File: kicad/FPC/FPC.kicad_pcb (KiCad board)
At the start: 2 copper layers, 29.3 x 5 mm, 2 parts, among them J1 Conn_01x04_Pin, J2 Conn_01x04_Pin

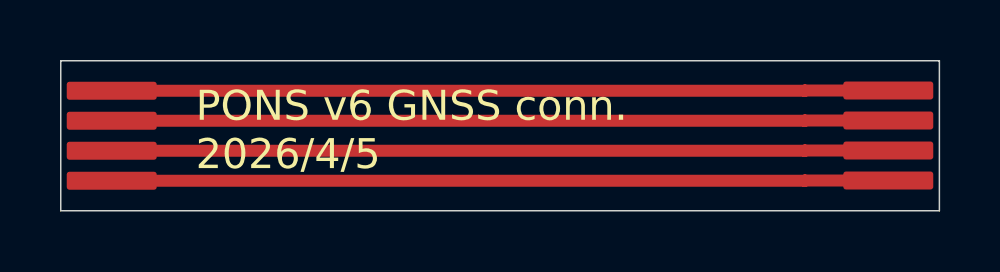
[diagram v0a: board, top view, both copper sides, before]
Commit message: 0.960 ソフトウェア＋ドキュメント KiCad v7 基板
普段編集しないモジュールを src/ へ移動し、README を v7 に更新

■ src/ への移動（Arduino IDE のタブ削減）
Arduino IDE はスケッチ直下のファイルを全部タブに出すため 28 個まで増え、
目的のファイルを探しづらくなっていた。仕様が固まっていて普段いじらない
4 モジュールを src/ へ移し、タブを 20 個に減らした。

  src/button.*     ボタン入力・メニュー
  src/sound.*      音声出力（WAV・トーン）
  src/vectormap.*  ベクタ地図の描画
  src/imulog.*     生 IMU ロガー

src/ 配下もコンパイルされるが IDE のタブには出ない。裏を返すと IDE からは
編集できなくなるので、これらは VSCode 等で編集すること。
またスケッチ直下は include パスに入っていないため、src/ の中からルート側の
ヘッダを参照するときは "../mysd.h" のように 1 段戻る必要がある。
この経緯と注意点は GPS_TFT_map.ino のヘッダに残した。

#include は 27 箇所を書き換え、全 104 件が実在するパスへ解決することを確認。

■ 併せて修正
button.cpp の #include "Button.h" が大文字始まりだった。macOS は
ファイルシステムが大文字小文字を区別しないため通っていたが、Linux では
壊れる。"button.h" に修正。

■ README を v7 に更新
 * タイトルとスペックを v7 へ。ソフトウェアバージョン 0.942 → 0.960
 * PONS Link（機体⇄ボート テレメトリ無線）の節を新設。3 台構成、下り一方向に
   した理由、無線パラメータ、実測 350m。設計の詳細は docs/pons_link.md へ
 * BNO085 を β 試験版から標準搭載へ。SPI 接続にした理由も記載
 * マイコンを RP2350B（外付け FLASH 16MB）と明記
 * PCBA とは別に発注する部品の一覧表（Digikey / マルツ / 秋月）を追加
 * 警告音・SD ログ・使用部品に無線関連を追記

重量とバッテリー持続時間は v7 実機での計測待ちのため、v6 β版の参考値と
PONS Link の消費電流だけを記載した。水面での到達距離も未確認と明記。

普段編集しないモジュールを src/ へ移動し、README を v7 に更新

■ src/ への移動（Arduino IDE のタブ削減）
Arduino IDE はスケッチ直下のファイルを全部タブに出すため 28 個まで増え、
目的のファイルを探しづらくなっていた。仕様が固まっていて普段いじらない
4 モジュールを src/ へ移し、タブを 20 個に減らした。

  src/button.*     ボタン入力・メニュー
  src/sound.*      音声出力（WAV・トーン）
  src/vectormap.*  ベクタ地図の描画
  src/imulog.*     生 IMU ロガー

src/ 配下もコンパイルされるが IDE のタブには出ない。裏を返すと IDE からは
編集できなくなるので、これらは VSCode 等で編集すること。
またスケッチ直下は include パスに入っていないため、src/ の中からルート側の
ヘッダを参照するときは "../mysd.h" のように 1 段戻る必要がある。
この経緯と注意点は GPS_TFT_map.ino のヘッダに残した。

#include は 27 箇所を書き換え、全 104 件が実在するパスへ解決することを確認。

■ 併せて修正
button.cpp の #include "Button.h" が大文字始まりだった。macOS は
ファイルシステムが大文字小文字を区別しないため通っていたが、Linux では
壊れる。"button.h" に修正。

■ README を v7 に更新
 * タイトルとスペックを v7 へ。ソフトウェアバージョン 0.942 → 0.960
 * PONS Link（機体⇄ボート テレメトリ無線）の節を新設。3 台構成、下り一方向に
   した理由、無線パラメータ、実測 350m。設計の詳細は docs/pons_link.md へ
 * BNO085 を β 試験版から標準搭載へ。SPI 接続にした理由も記載
 * マイコンを RP2350B（外付け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
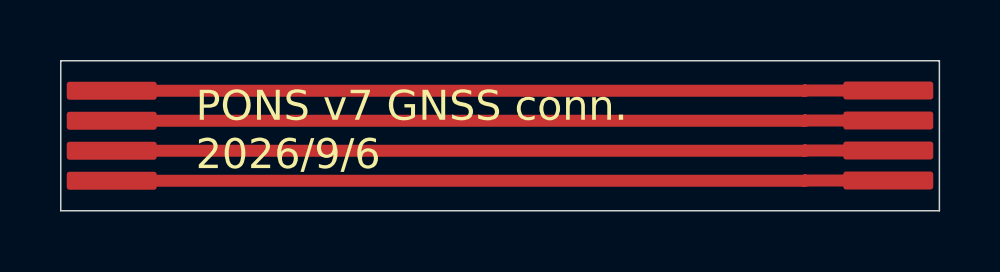
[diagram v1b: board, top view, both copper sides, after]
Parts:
- J1, J2: footprint PONS:FPC_CON 4 POS 1mm -> FPC_CON 4p 1mm:FPC_CON 4p 1mm
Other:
- board text added: "PONS v7 GNSS conn. 2026/9/6"
- board text added: "Stiffener: Polyimide Thickness: 0.3mm"
- board text removed: "PONS v6 GNSS conn. 2026/4/5"
- board text removed: "Stiffener: Polyimide Thickness: 0.25mm or 0.3mm"
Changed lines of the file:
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@@
 (kicad_pcb
-	(version 20241229)
+	(version 20260206)
 	(generator "pcbnew")
-	(generator_version "9.0")
+	(generator_version "10.0")
 	(general
 		(thickness 1.6)
@@
 	)
 	(paper "A4")
+	(title_block
+		(title "FPC for PONS v7")
+		(date "2026-09-06")
+		(rev "v7")
+		(comment 1 "EXPORT Stiffener AND User.Comments for JLCPCB")
+	)
 	(layers
 		(0 "F.Cu" signal)
@@
 		(pad_to_mask_clearance 0)
 		(allow_soldermask_bridges_in_footprints no)
-		(tenting front back)
+		(tenting
+			(front yes)
+			(back yes)
+		)
+		(covering
+			(front no)
+			(back no)
+		)
+		(plugging
+			(front no)
+			(back no)
+		)
+		(capping no)
+		(filling no)
 		(pcbplotparams
 			(layerselection 0x00000000_00000000_5555d555_5755f5ff)
@@
 			(usegerberadvancedattributes no)
 			(creategerberjobfile no)
-			(dashed_line_dash_ratio 12.000000)
-			(dashed_line_gap_ratio 3.000000)
+			(dashed_line_dash_ratio 12)
+			(dashed_line_gap_ratio 3)
 			(svgprecision 4)
 			(plotframeref no)
 			(mode 1)
 			(useauxorigin no)
-			(hpglpennumber 1)
-			(hpglpenspeed 20)
-			(hpglpendiameter 15.000000)
 			(pdf_front_fp_property_popups yes)
 			(pdf_back_fp_property_popups yes)
@@
 		)
 	)
-	(net 0 "")
-	(net 1 "Net-(J1-Pin_4)")
-	(net 2 "Net-(J1-Pin_1)")
-	(net 3 "Net-(J1-Pin_3)")
-	(net 4 "Net-(J1-Pin_2)")
-	(footprint "PONS:FPC_CON 4 POS 1mm"
+	(footprint "FPC_CON 4p 1mm:FPC_CON 4p 1mm"
 		(layer "F.Cu")
 		(at 120.6 66.2)
@@
 			)
 		)
-		(property "Datasheet" "~"
+		(property "Datasheet" ""
 			(at 0 0 0)
 			(unlocked yes)
@@
 		(sheetname "/")
 		(sheetfile "FPC.kicad_sch")
+		(units
+			(unit
+				(name "A")
+				(pins "1" "2" "3" "4")
+			)
+		)
 		(attr smd)
+		(duplicate_pad_numbers_are_jumpers no)
 		(fp_text user "${REFERENCE}"
 			(at 0 2.5 0)
@@
 			(layers "F.Cu" "F.Mask" "F.Paste")
 			(roundrect_rratio 0.15)
-			(net 2 "Net-(J1-Pin_1)")
-			(pinfunction "Pin_1")
+			(net "Net-(J1-Pin_1)")
+			(pinfunction "Pin_1_1")
 			(pintype "passive")
 		)
@@
 			(layers "F.Cu" "F.Mask" "F.Paste")
 			(roundrect_rratio 0.15)
-			(net 4 "Net-(J1-Pin_2)")
-			(pinfunction "Pin_2")
+			(net "Net-(J1-Pin_2)")
+			(pinfunction "Pin_2_2")
 			(pintype "passive")
 		)
@@
 			(layers "F.Cu" "F.Mask" "F.Paste")
 			(roundrect_rratio 0.15)
-			(net 3 "Net-(J1-Pin_3)")
-			(pinfunction "Pin_3")
+			(net "Net-(J1-Pin_3)")
+			(pinfunction "Pin_3_3")
 			(pintype "passive")
 		)
@@
 			(layers "F.Cu" "F.Mask" "F.Paste")
 			(roundrect_rratio 0.15)
-			(net 1 "Net-(J1-Pin_4)")
-			(pinfunction "Pin_4")
+			(net "Net-(J1-Pin_4)")
+			(pinfunction "Pin_4_4")
 			(pintype "passive")
 		)
 		(embedded_fonts no)
 	)
-	(footprint "PONS:FPC_CON 4 POS 1mm"
+	(footprint "FPC_CON 4p 1mm:FPC_CON 4p 1mm"
 		(layer "F.Cu")
 		(at 146.4836 66.1924)
@@
 			)
 		)
-		(property "Datasheet" "~"
+		(property "Datasheet" ""
 			(at 0 0 0)
 			(unlocked yes)
@@
 		(sheetname "/")
 		(sheetfile "FPC.kicad_sch")
+		(units
+			(unit
+				(name "A")
+				(pins "1" "2" "3" "4")
+			)
+		)
 		(attr smd)
+		(duplicate_pad_numbers_are_jumpers no)
 		(fp_text user "${REFERENCE}"
 			(at 0 2.5 0)
@@
 			(layers "F.Cu" "F.Mask" "F.Paste")
 			(roundrect_rratio 0.15)
-			(net 2 "Net-(J1-Pin_1)")
-			(pinfunction "Pin_1")
+			(net "Net-(J1-Pin_1)")
+			(pinfunction "Pin_1_1")
 			(pintype "passive")
 		)
@@
 			(layers "F.Cu" "F.Mask" "F.Paste")
 			(roundrect_rratio 0.15)
-			(net 4 "Net-(J1-Pin_2)")
-			(pinfunction "Pin_2")
+			(net "Net-(J1-Pin_2)")
+			(pinfunction "Pin_2_2")
 			(pintype "passive")
 		)
@@
 			(layers "F.Cu" "F.Mask" "F.Paste")
 			(roundrect_rratio 0.15)
-			(net 3 "Net-(J1-Pin_3)")
-			(pinfunction "Pin_3")
+			(net "Net-(J1-Pin_3)")
+			(pinfunction "Pin_3_3")
 			(pintype "passive")
 		)
@@
 			(layers "F.Cu" "F.Mask" "F.Paste")
 			(roundrect_rratio 0.15)
-			(net 1 "Net-(J1-Pin_4)")
-			(pinfunction "Pin_4")
+			(net "Net-(J1-Pin_4)")
+			(pinfunction "Pin_4_4")
 			(pintype "passive")
 		)
@@
 	)
 	(gr_rect
+		(start 118.9 63.7)
+		(end 123.4 68.7)
+		(stroke
+			(width 0.1)
+			(type solid)
+		)
+		(fill no)
+		(layer "User.5")
+	)
+	(gr_rect
 		(start 143.6836 63.6924)
 		(end 148.1836 68.6924)
@@
 		(layer "User.5")
 	)
-	(gr_rect
-		(start 118.9 63.7)
-		(end 123.4 68.7)
-		(stroke
-			(width 0.1)
-			(type solid)
-		)
-		(fill no)
-		(layer "User.5")
-	)
-	(gr_text "PONS v6 GNSS conn.\n2026/4/5"
+	(gr_text "PONS v7 GNSS conn.\n2026/9/6"
 		(at 123.4 67.4 0)
 		(layer "F.SilkS")
@@
 		)
 	)
-	(gr_text "Stiffener: Polyimide\nThickness: 0.25mm or 0.3mm"
+	(gr_text "Stiffener: Polyimide\nThickness: 0.3mm"
 		(at 125.4 72.1 0)
-		(layer "User.5")
+		(layer "Cmts.User")
 		(effects
 			(font
@@
 	)
 	(segment
+		(start 146.4836 64.6924)
+		(end 143.7076 64.6924)
+		(width 0.4)
+		(layer "F.Cu")
+		(net "Net-(J1-Pin_1)")
+	)
+	(segment
+		(start 120.4 64.7)
+		(end 143.7 64.7)
+		(width 0.4)
+		(layer "F.Cu")
+		(net "Net-(J1-Pin_1)")
+	)
+	(segment
+		(start 143.7076 64.6924)
+		(end 143.7 64.7)
+		(width 0.4)
+		(layer "F.Cu")
+		(net "Net-(J1-Pin_1)")
+	)
+	(segment
+		(start 143.7076 65.6924)
+		(end 146.4836 65.6924)
+		(width 0.4)
+		(layer "F.Cu")
+		(net "Net-(J1-Pin_2)")
+	)
+	(segment
+		(start 143.7 65.7)
+		(end 120.4 65.7)
+		(width 0.4)
+		(layer "F.Cu")
+		(net "Net-(J1-Pin_2)")
+	)
+	(segment
+		(start 143.7 65.7)
+		(end 143.7076 65.6924)
+		(width 0.4)
+		(layer "F.Cu")
+		(net "Net-(J1-Pin_2)")
+	)
+	(segment
+		(start 120.4 66.7)
+		(end 143.7 66.7)
+		(width 0.4)
+		(layer "F.Cu")
+		(net "Net-(J1-Pin_3)")
+	)
+	(segment
+		(start 146.4836 66.6924)
+		(end 143.7076 66.6924)
+		(width 0.4)
+		(layer "F.Cu")
+		(net "Net-(J1-Pin_3)")
+	)
+	(segment
+		(start 143.7076 66.6924)
+		(end 143.7 66.7)
+		(width 0.4)
+		(layer "F.Cu")
+		(net "Net-(J1-Pin_3)")
+	)
+	(segment
 		(start 143.7076 67.6924)
 		(end 146.4836 67.6924)
 		(width 0.4)
 		(layer "F.Cu")
-		(net 1)
+		(net "Net-(J1-Pin_4)")
 	)
 	(segment
@@
 		(width 0.4)
 		(layer "F.Cu")
-		(net 1)
+		(net "Net-(J1-Pin_4)")
 	)
 	(segment
@@
 		(width 0.4)
 		(layer "F.Cu")
-		(net 1)
-	)
-	(segment
-		(start 146.4836 64.6924)
-		(end 143.7076 64.6924)
-		(width 0.4)
-		(layer "F.Cu")
-		(net 2)
-	)
-	(segment
-		(start 120.4 64.7)
-		(end 143.7 64.7)
-		(width 0.4)
-		(layer "F.Cu")
-		(net 2)
-	)
-	(segment
-		(start 143.7076 64.6924)
-		(end 143.7 64.7)
-		(width 0.4)
-		(layer "F.Cu")
-		(net 2)
-	)
-	(segment
-		(start 120.4 66.7)
-		(end 143.7 66.7)
-		(width 0.4)
-		(layer "F.Cu")
-		(net 3)
-	)
-	(segment
-		(start 146.4836 66.6924)
-		(end 143.7076 66.6924)
-		(width 0.4)
-		(layer "F.Cu")
-		(net 3)
-	)
-	(segment
-		(start 143.7076 66.6924)
-		(end 143.7 66.7)
-		(width 0.4)
-		(layer "F.Cu")
-		(net 3)
-	)
-	(segment
-		(start 143.7076 65.6924)
-		(end 146.4836 65.6924)
-		(width 0.4)
-		(layer "F.Cu")
-		(net 4)
-	)
-	(segment
-		(start 143.7 65.7)
-		(end 120.4 65.7)
-		(width 0.4)
-		(layer "F.Cu")
-		(net 4)
-	)
-	(segment
-		(start 143.7 65.7)
-		(end 143.7076 65.6924)
-		(width 0.4)
-		(layer "F.Cu")
-		(net 4)
+		(net "Net-(J1-Pin_4)")
 	)
 	(embedded_fonts no)

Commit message: 0.961 KiCad更新 wav更新
wav雑音除去
kicad更新（スイッチ背面、DocへのQRコード更新）
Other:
- board text added: "Total Thickness: 0.3mm (Polyimide Stiffener 0.25mm)"
- board text removed: "Stiffener: Polyimide Thickness: 0.3mm"
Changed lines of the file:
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@@
 		)
 	)
-	(gr_text "Stiffener: Polyimide\nThickness: 0.3mm"
-		(at 125.4 72.1 0)
+	(gr_text "Total Thickness: 0.3mm (Polyimide Stiffener 0.25mm)"
+		(at 115.65 72.6 0)
 		(layer "Cmts.User")
 		(effects
